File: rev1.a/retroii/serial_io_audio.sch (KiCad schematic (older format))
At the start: 49 parts, among them J13 74LS74, J14 Game_IO_Socket, J2 Joystick 1, J3 Joystick 2, J4 PC Port 1, J5 PC Port 2, J6 Edge mounted connector, J7 Cassette In, J8 Cassette Out, J9 Speaker Jack, K13 LM741, Q4 MPSA13

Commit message: added audio logarithmic volume control
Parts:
- C5, C6, C7, C8: footprint (none) -> Capacitor_THT:C_Disc_D3.4mm_W2.1mm_P2.50mm
- RV1: footprint (none) -> retroii_footprints:BOURNS_91A1A-B24-D15L
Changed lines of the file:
@@
 F 0 "C8" H 3375 4715 50  0000 L CNN
 F 1 ".022uF" V 3315 4680 50  0000 L CNN
-F 2 "" H 3370 4655 50  0001 C CNN
+F 2 "Capacitor_THT:C_Disc_D3.4mm_W2.1mm_P2.50mm" H 3370 4655 50  0001 C CNN
 F 3 "~" H 3370 4655 50  0001 C CNN
 	1    3370 4655
@@
 F 0 "C5" H 3235 5365 50  0000 L CNN
 F 1 ".022uF" V 3175 5330 50  0000 L CNN
-F 2 "" H 3230 5305 50  0001 C CNN
+F 2 "Capacitor_THT:C_Disc_D3.4mm_W2.1mm_P2.50mm" H 3230 5305 50  0001 C CNN
 F 3 "~" H 3230 5305 50  0001 C CNN
 	1    3230 5305
@@
 F 0 "C6" H 3095 5965 50  0000 L CNN
 F 1 ".022uF" V 3035 5930 50  0000 L CNN
-F 2 "" H 3090 5905 50  0001 C CNN
+F 2 "Capacitor_THT:C_Disc_D3.4mm_W2.1mm_P2.50mm" H 3090 5905 50  0001 C CNN
 F 3 "~" H 3090 5905 50  0001 C CNN
 	1    3090 5905
@@
 F 0 "C7" H 2955 6565 50  0000 L CNN
 F 1 ".022uF" V 2895 6530 50  0000 L CNN
-F 2 "" H 2950 6505 50  0001 C CNN
+F 2 "Capacitor_THT:C_Disc_D3.4mm_W2.1mm_P2.50mm" H 2950 6505 50  0001 C CNN
 F 3 "~" H 2950 6505 50  0001 C CNN
 	1    2950 6505
@@
 F 0 "RV1" H 10070 4471 50  0000 R CNN
 F 1 "Volume" H 10275 4630 50  0000 R CNN
-F 2 "" H 10140 4425 50  0001 C CNN
+F 2 "retroii_footprints:BOURNS_91A1A-B24-D15L" H 10140 4425 50  0001 C CNN
 F 3 "~" H 10140 4425 50  0001 C CNN
 	1    10140 4425

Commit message: added 8ohm speaker footprint and 3d model
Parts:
- LS1: footprint (none) -> retroii_footprints:CUI_CVI_1708
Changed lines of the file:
@@
 F 0 "LS1" H 10510 4766 50  0000 L CNN
 F 1 "Speaker" H 10270 4970 50  0000 L CNN
-F 2 "" H 10340 4570 50  0001 C CNN
+F 2 "retroii_footprints:CUI_CVI_1708" H 10340 4570 50  0001 C CNN
 F 3 "~" H 10330 4720 50  0001 C CNN
 	1    10340 4770

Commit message: added audio connector footprints/3d models.
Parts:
- added J24: Headphone, retroii_footprints:SJ13525NHeadphone, symbol retroii:AudioJack2_Ground
- added JP16, JP17, JP18, JP19: Jumper_NC_Small, Connector_PinHeader_2.54mm:PinHeader_1x02_P2.54mm_Vertical, symbol Device:Jumper_NC_Small
- J7, J8: footprint (none) -> retroii_footprints:SJ13525NHeadphone; symbol Connector:AudioJack2 -> retroii:AudioJack2_Ground
- J9: footprint (none) -> Connector_PinSocket_2.54mm:PinSocket_1x02_P2.54mm_Vertical
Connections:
- wire segments 194 -> 212
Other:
- moved on the sheet: LS1, RV1
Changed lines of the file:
@@
 L Device:Speaker LS1
 U 1 1 5C8B0058
-P 10340 4770
-F 0 "LS1" H 10510 4766 50  0000 L CNN
-F 1 "Speaker" H 10270 4970 50  0000 L CNN
-F 2 "retroii_footprints:CUI_CVI_1708" H 10340 4570 50  0001 C CNN
-F 3 "~" H 10330 4720 50  0001 C CNN
-	1    10340 4770
+P 10695 4770
+F 0 "LS1" H 10865 4766 50  0000 L CNN
+F 1 "Speaker" H 10625 4970 50  0000 L CNN
+F 2 "retroii_footprints:CUI_CVI_1708" H 10695 4570 50  0001 C CNN
+F 3 "~" H 10685 4720 50  0001 C CNN
+	1    10695 4770
 	1    0    0    -1
 $EndComp
@@
 $EndComp
 $Comp
-L Connector:AudioJack2 J8
+L retroii:AudioJack2_Ground J8
 U 1 1 5C8B0BBB
 P 9455 4810
 F 0 "J8" H 9275 4793 50  0000 R CNN
-F 1 "Cassette Out" H 9605 4640 50  0000 R CNN
-F 2 "" H 9455 4810 50  0001 C CNN
+F 1 "Cassette Out" H 9445 4675 50  0000 R CNN
+F 2 "retroii_footprints:SJ13525NHeadphone" H 9455 4810 50  0001 C CNN
 F 3 "~" H 9455 4810 50  0001 C CNN
 	1    9455 4810
@@
 $EndComp
 $Comp
-L Connector:AudioJack2 J7
+L retroii:AudioJack2_Ground J7
 U 1 1 5C8B71E8
 P 6760 3395
 F 0 "J7" H 6675 3590 50  0000 C CNN
-F 1 "Cassette In" H 6760 3260 50  0000 C CNN
-F 2 "" H 6760 3395 50  0001 C CNN
+F 1 "Cassette In" H 6975 3260 50  0000 C CNN
+F 2 "retroii_footprints:SJ13525NHeadphone" H 6760 3395 50  0001 C CNN
 F 3 "~" H 6760 3395 50  0001 C CNN
 	1    6760 3395
@@
 	10140 5110 10140 5180
 Wire Wire Line
-	10140 4870 10140 5110
+	10140 4870 10140 4960
 Wire Wire Line
 	9595 6120 9595 6215
@@
 	9255 4910 9160 4910
 Wire Wire Line
-	9160 4910 9160 5220
-Wire Wire Line
-	9160 5220 8950 5220
-Wire Wire Line
-	8950 5220 8950 5250
-Wire Wire Line
-	8950 5190 8950 5220
-Connection ~ 8950 5220
-Wire Wire Line
-	9255 4810 8950 4810
+	9255 4810 9160 4810
 Wire Wire Line
 	8950 4890 8950 4810
@@
 Wire Wire Line
 	8540 4810 8445 4810
-Text Label 10525 4425 2    50   ~ 0
+Text Label 10585 3880 2    50   ~ 0
 +5V
 $Comp
@@
 Wire Wire Line
 	6960 3495 7025 3495
-Wire Wire Line
-	7025 3495 7025 3595
-$Comp
-L 6502Bootstrapper-cache:GND #PWR046
-U 1 1 5C8E3F73
-P 7025 3595
-F 0 "#PWR046" H 7025 3345 50  0001 C CNN
-F 1 "GND" H 7030 3422 50  0000 C CNN
-F 2 "" H 7025 3595 60  0000 C CNN
-F 3 "" H 7025 3595 60  0000 C CNN
-	1    7025 3595
-	1    0    0    -1
-$EndComp
 Wire Wire Line
 	7295 3395 7465 3395
@@
 $EndComp
 Wire Wire Line
-	7095 3395 6960 3395
+	7095 3395 7025 3395
 Wire Wire Line
 	4690 3675 4690 3505
@@
 L Device:R_POT RV1
 U 1 1 5C9EC141
-P 10140 4425
-F 0 "RV1" H 10070 4471 50  0000 R CNN
-F 1 "Volume" H 10275 4630 50  0000 R CNN
-F 2 "retroii_footprints:BOURNS_91A1A-B24-D15L" H 10140 4425 50  0001 C CNN
-F 3 "~" H 10140 4425 50  0001 C CNN
-	1    10140 4425
-	1    0    0    -1
-$EndComp
-Wire Wire Line
-	10140 4575 10140 4770
-Wire Wire Line
-	10290 4425 10525 4425
+P 10200 3880
+F 0 "RV1" H 10130 3926 50  0000 R CNN
+F 1 "Volume" H 10335 4085 50  0000 R CNN
+F 2 "retroii_footprints:BOURNS_91A1A-B24-D15L" H 10200 3880 50  0001 C CNN
+F 3 "~" H 10200 3880 50  0001 C CNN
+	1    10200 3880
+	1    0    0    -1
+$EndComp
+Wire Wire Line
+	10350 3880 10585 3880
 Text Label 3370 3020 1    50   ~ 0
 PDL0
@@
 F 0 "J9" H 9860 4545 50  0000 C CNN
 F 1 "Speaker Jack" H 10000 4970 50  0000 C CNN
-F 2 "" H 9940 4870 50  0001 C CNN
+F 2 "Connector_PinSocket_2.54mm:PinSocket_1x02_P2.54mm_Vertical" H 9940 4870 50  0001 C CNN
 F 3 "~" H 9940 4870 50  0001 C CNN
 	1    9940 4870
 	-1   0    0    1
 $EndComp
-Connection ~ 10140 4870
-Connection ~ 10140 4770
 NoConn ~ 8160 3595
 NoConn ~ 8260 3595
@@
 Wire Wire Line
 	10590 3095 10370 3095
-NoConn ~ 10140 4275
+NoConn ~ 10200 3730
 $Comp
 L 6502:R R56
@@
 Wire Wire Line
 	8145 5210 8145 5540
+$Comp
+L Device:Jumper_NC_Small JP19
+U 1 1 5CBF9D7F
+P 10345 4870
+F 0 "JP19" H 10345 4820 50  0000 C CNN
+F 1 "Jumper_NC_Small" H 10415 4745 50  0001 C CNN
+F 2 "Connector_PinHeader_2.54mm:PinHeader_1x02_P2.54mm_Vertical" H 10345 4870 50  0001 C CNN
+F 3 "~" H 10345 4870 50  0001 C CNN
+	1    10345 4870
+	1    0    0    -1
+$EndComp
+Wire Wire Line
+	10495 4870 10445 4870
+Wire Wire Line
+	10245 4870 10140 4870
+Connection ~ 10140 4870
+$Comp
+L retroii:AudioJack2_Ground J24
+U 1 1 5CC45BFD
+P 10460 4355
+F 0 "J24" H 10440 4215 50  0000 R CNN
+F 1 "Headphone" H 10340 4195 50  0000 R CNN
+F 2 "retroii_footprints:SJ13525NHeadphone" H 10460 4355 50  0001 C CNN
+F 3 "~" H 10460 4355 50  0001 C CNN
+	1    10460 4355
+	-1   0    0    1
+$EndComp
+Wire Wire Line
+	9455 4610 9455 4580
+$Comp
+L 6502Bootstrapper-cache:GND #PWR092
+U 1 1 5CC677A5
+P 9455 4580
+F 0 "#PWR092" H 9455 4330 50  0001 C CNN
+F 1 "GND" H 9455 4455 50  0000 C CNN
+F 2 "" H 9455 4580 60  0000 C CNN
+F 3 "" H 9455 4580 60  0000 C CNN
+	1    9455 4580
+	-1   0    0    1
+$EndComp
+Wire Wire Line
+	6760 3195 6760 3165
+$Comp
+L 6502Bootstrapper-cache:GND #PWR046
+U 1 1 5CC7531B
+P 6760 3165
+F 0 "#PWR046" H 6760 2915 50  0001 C CNN
+F 1 "GND" H 6760 3030 50  0000 C CNN
+F 2 "" H 6760 3165 60  0000 C CNN
+F 3 "" H 6760 3165 60  0000 C CNN
+	1    6760 3165
+	-1   0    0    1
+$EndComp
+Wire Wire Line
+	7025 3495 7025 3395
+Connection ~ 7025 3395
+Wire Wire Line
+	7025 3395 6960 3395
+Wire Wire Line
+	8950 5190 8950 5250
+Wire Wire Line
+	9160 4910 9160 4810
+Connection ~ 9160 4810
+Wire Wire Line
+	9160 4810 8950 4810
+Wire Wire Line
+	10140 4960 10210 4960
+Wire Wire Line
+	10210 4355 10260 4355
+Connection ~ 10140 4960
+Wire Wire Line
+	10140 4960 10140 5110
+Wire Wire Line
+	10260 4455 10210 4455
+Wire Wire Line
+	10210 4455 10210 4355
+Wire Wire Line
+	10140 4145 10200 4145
+Wire Wire Line
+	10200 4145 10200 4030
+Wire Wire Line
+	10140 4145 10140 4770
+$Comp
+L Device:Jumper_NC_Small JP17
+U 1 1 5CCD942F
+P 10330 4145
+F 0 "JP17" H 10330 4095 50  0000 C CNN
+F 1 "Jumper_NC_Small" H 10400 4020 50  0001 C CNN
+F 2 "Connector_PinHeader_2.54mm:PinHeader_1x02_P2.54mm_Vertical" H 10330 4145 50  0001 C CNN
+F 3 "~" H 10330 4145 50  0001 C CNN
+	1    10330 4145
+	1    0    0    -1
+$EndComp
+Wire Wire Line
+	10460 4155 10460 4145
+Wire Wire Line
+	10460 4145 10430 4145
+Wire Wire Line
+	10230 4145 10200 4145
+Connection ~ 10200 4145
+$Comp
+L Device:Jumper_NC_Small JP16
+U 1 1 5CCF7132
+P 10210 4605
+F 0 "JP16" H 10215 4690 50  0000 C CNN
+F 1 "Jumper_NC_Small" H 10280 4480 50  0001 C CNN
+F 2 "Connector_PinHeader_2.54mm:PinHeader_1x02_P2.54mm_Vertical" H 10210 4605 50  0001 C CNN
+F 3 "~" H 10210 4605 50  0001 C CNN
+	1    10210 4605
+	0    1    1    0
+$EndComp
+Wire Wire Line
+	10210 4505 10210 4455
+Connection ~ 10210 4455
+Wire Wire Line
+	10210 4705 10210 4960
+$Comp
+L Device:Jumper_NC_Small JP18
+U 1 1 5CD165ED
+P 10345 4770
+F 0 "JP18" H 10345 4720 50  0000 C CNN
+F 1 "Jumper_NC_Small" H 10415 4645 50  0001 C CNN
+F 2 "Connector_PinHeader_2.54mm:PinHeader_1x02_P2.54mm_Vertical" H 10345 4770 50  0001 C CNN
+F 3 "~" H 10345 4770 50  0001 C CNN
+	1    10345 4770
+	1    0    0    -1
+$EndComp
+Wire Wire Line
+	10445 4770 10495 4770
+Wire Wire Line
+	10245 4770 10140 4770
 Wire Bus Line
 	10690 2755 10690 3195
+Connection ~ 10140 4770
 $EndSCHEMATC

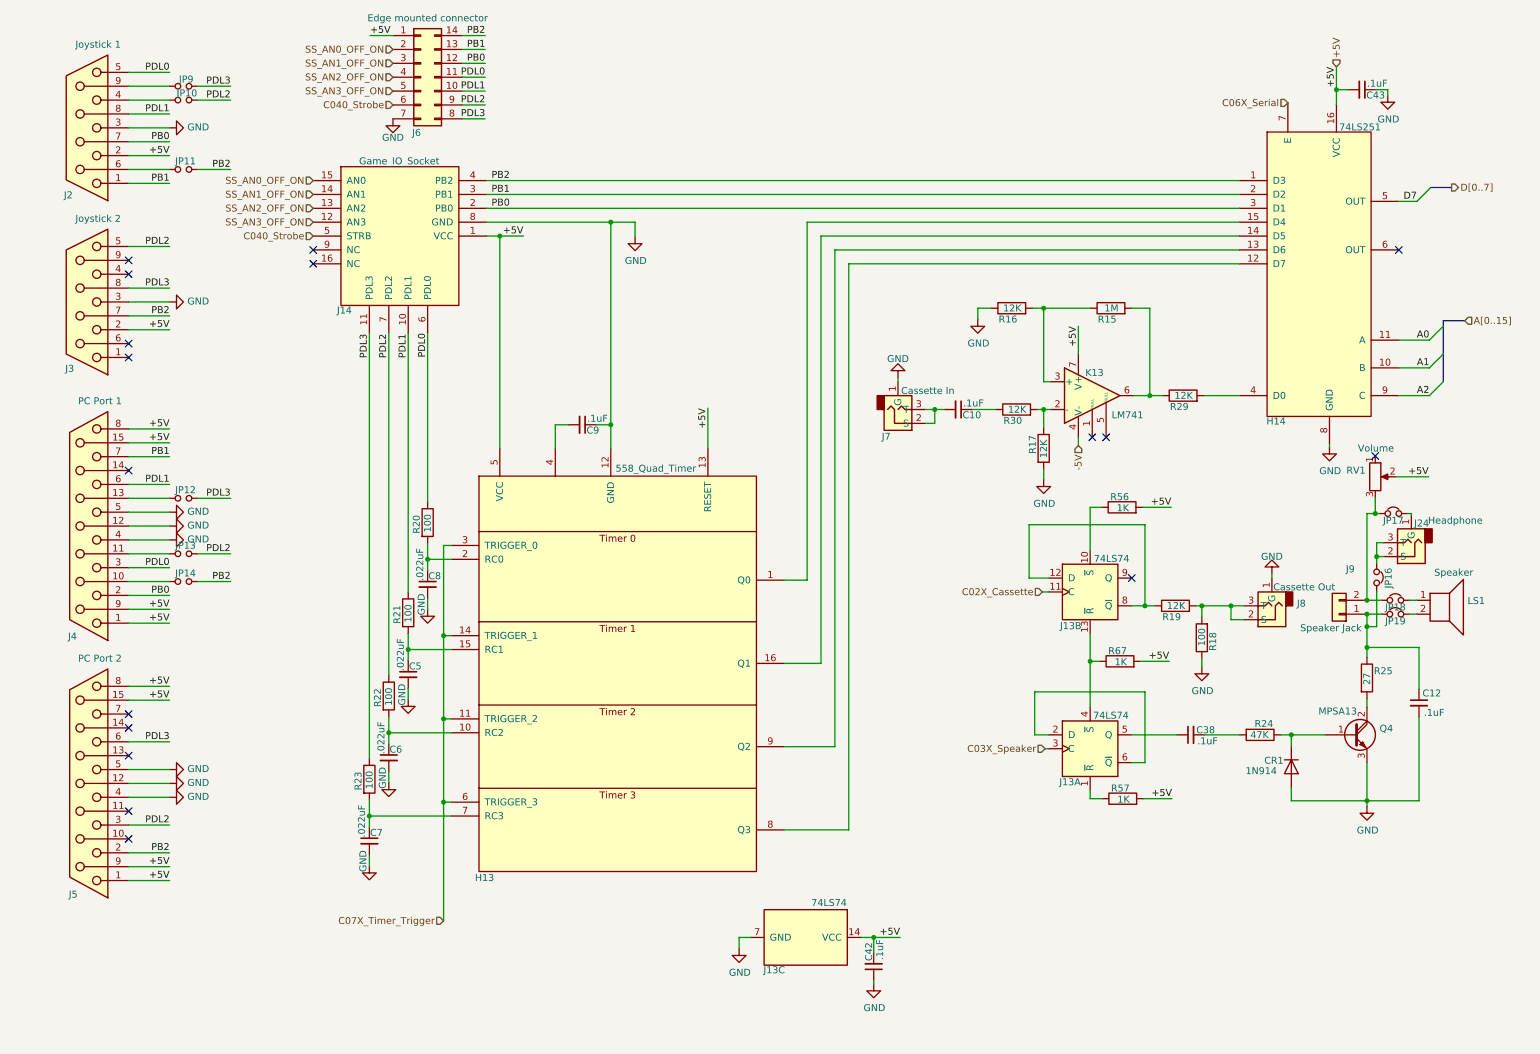
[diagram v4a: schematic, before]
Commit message: replaced 558 quad timer with 2 556 dual timers.
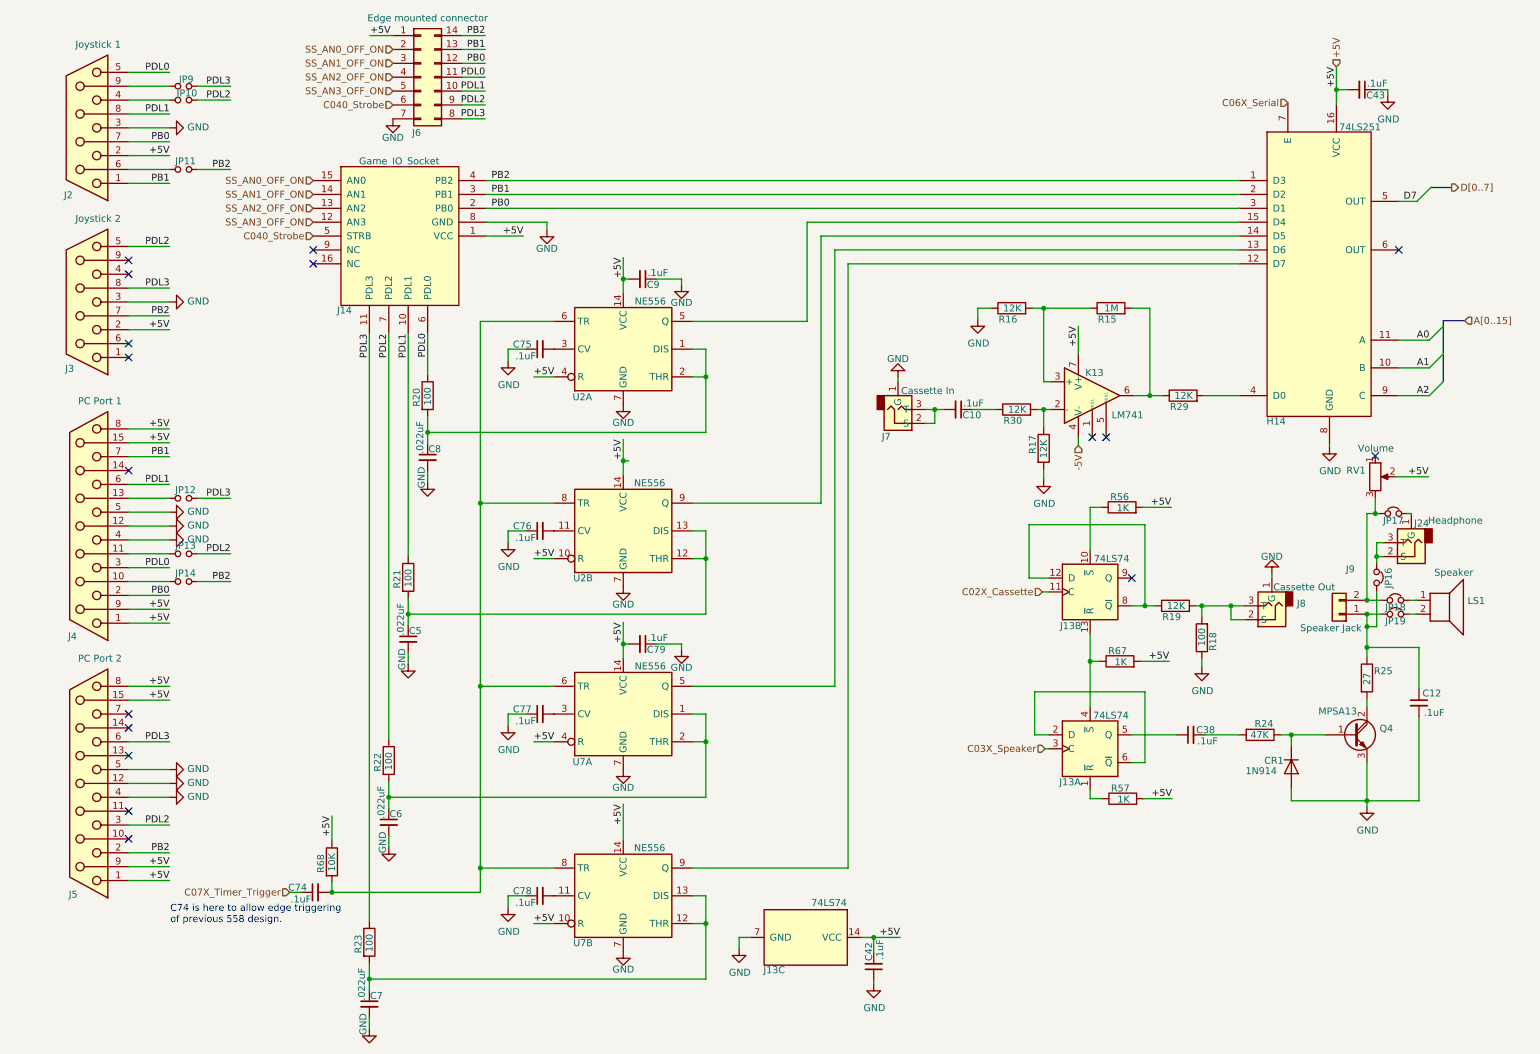
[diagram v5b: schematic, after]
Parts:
- removed H13: 558_Quad_Timer, retroii_footprints:DIP-16_W7.62mm_Socket_LongPads, symbol retroii:558_Quad_Timer
- added C74, C75, C76, C77, C78, C79: .1uF, retroii_footprints:C_Disc_D3.0mm_W2.0mm_P2.50mm, symbol Device:C_Small
- added R68: 10K, retroii_footprints:R_Axial_DIN0207_L6.3mm_D2.5mm_P10.16mm_Horizontal, symbol 6502:R
- added U2, U7: NE556, retroii_footprints:DIP-14_W7.62mm_Socket_LongPads, symbol Timer:NE556
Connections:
- net +5V: now also C9.2, C79.2, R68.1, U2.10 (R), U2.14 (VCC), U2.14 (VCC), U2.4 (R), U7.10 (R), U7.14 (VCC), U7.14 (VCC), U7.4 (R)
- net C07X_Timer_Trigger: now also C74.1
- net GND: now also C75.1, C76.1, C77.1, C78.1, C79.1, U2.7 (GND), U2.7 (GND), U7.7 (GND), U7.7 (GND)
- net at H14.15 (D4): now also U2.5 (Q)
- net at C6.1, R22.2: now also U7.1 (DIS), U7.2 (THR)
- net at C5.1, R21.2: now also U2.12 (THR), U2.13 (DIS)
- net at H14.14 (D5): now also U2.9 (Q)
- net at C8.1, R20.2: now also U2.1 (DIS), U2.2 (THR)
- net at C7.1, R23.2: now also U7.12 (THR), U7.13 (DIS)
- net at H14.12 (D7): now also U7.9 (Q)
- net at H14.13 (D6): now also U7.5 (Q)
- new net: C75.2, U2.3 (CV)
- new net: C74.2, R68.2, U2.6 (TR), U2.8 (TR), U7.6 (TR), U7.8 (TR)
- new net: C76.2, U2.11 (CV)
- new net: C77.2, U7.3 (CV)
- new net: C78.2, U7.11 (CV)
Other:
- note added: "C74 is here to allow edge triggering\nof previous 558 design."
- moved on the sheet: C5, C6, C7, C8, C9, R20, R21, R22, R23
